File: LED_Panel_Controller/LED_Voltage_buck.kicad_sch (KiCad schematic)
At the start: 11 parts, among them U10 LM2596S-ADJ

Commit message: changed page size, BOM
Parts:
- U10: Digikey 4518-LM2596S-ADJCT-ND -> https://www.amazon.com/gp/product/B0B63GQDJW/
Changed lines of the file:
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@@
       (effects (font (size 1.27 1.27)) hide)
     )
-    (property "Digikey" "4518-LM2596S-ADJCT-ND" (id 4) (at 127 64.77 0)
+    (property "Digikey" "https://www.amazon.com/gp/product/B0B63GQDJW/" (id 4) (at 127 64.77 0)
       (effects (font (size 1.27 1.27)) hide)
     )

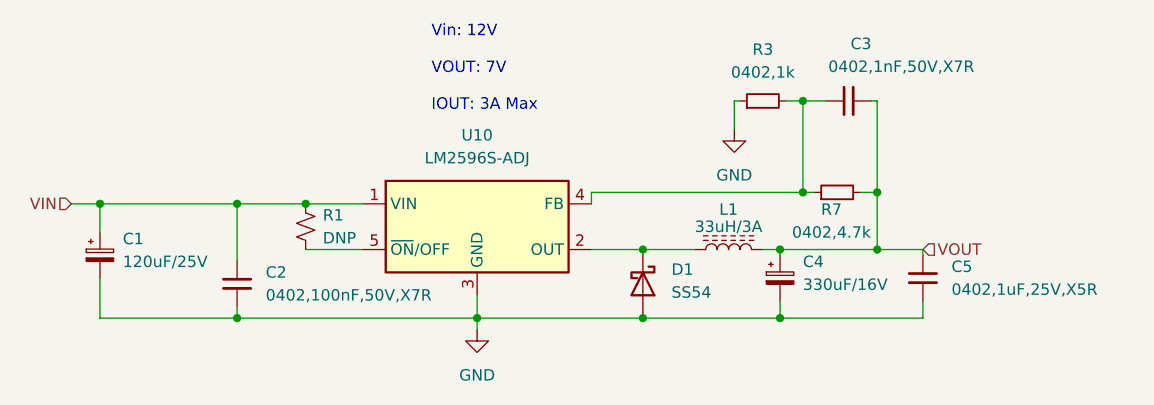
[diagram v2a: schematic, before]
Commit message: changed VIN cap to 35V rating
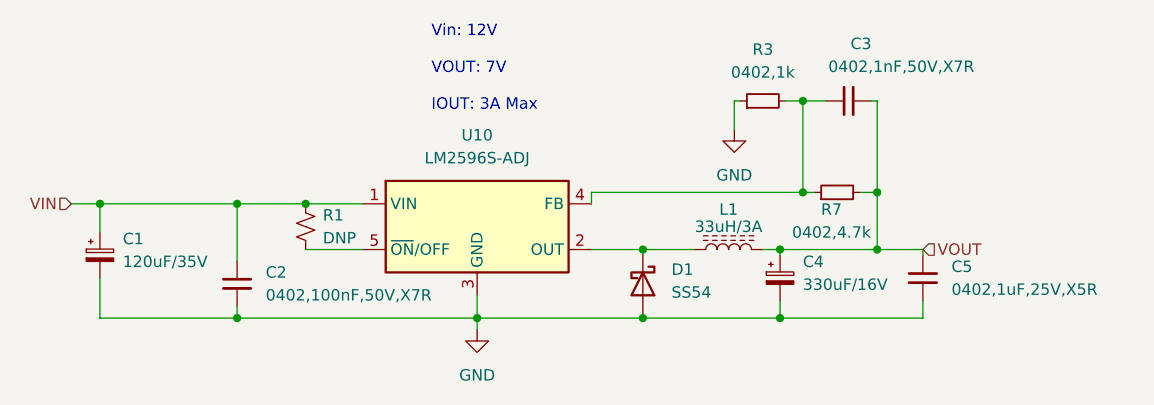
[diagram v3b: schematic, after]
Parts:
- C1: value 120uF/25V -> 120uF/35V; Digikey 732-8632-1-ND -> 1189-3657-ND; MFGPN 860010473009 -> 35ZLQ120MEFC6.3X11
- C4: Digikey 732-8798-1-ND -> 399-ESK337M016AE3AA-ND; MFGPN 860020373011 -> ESK337M016AE3AA
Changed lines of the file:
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@@
       (effects (font (size 1.27 1.27)) (justify left))
     )
-    (property "Value" "120uF/25V" (id 1) (at 87.63 68.6688 0)
+    (property "Value" "120uF/35V" (id 1) (at 87.63 68.6688 0)
       (effects (font (size 1.27 1.27)) (justify left))
     )
@@
       (effects (font (size 1.27 1.27)) hide)
     )
-    (property "Digikey" "732-8632-1-ND" (id 4) (at 85.09 67.945 0)
+    (property "Digikey" "1189-3657-ND" (id 4) (at 85.09 67.945 0)
       (effects (font (size 1.27 1.27)) hide)
     )
-    (property "MFGPN" "860010473009" (id 5) (at 85.09 67.945 0)
+    (property "MFGPN" "35ZLQ120MEFC6.3X11" (id 5) (at 85.09 67.945 0)
       (effects (font (size 1.27 1.27)) hide)
     )
@@
       (effects (font (size 1.27 1.27)) hide)
     )
-    (property "Digikey" "732-8798-1-ND" (id 4) (at 160.655 70.485 0)
+    (property "Digikey" "399-ESK337M016AE3AA-ND" (id 4) (at 160.655 70.485 0)
       (effects (font (size 1.27 1.27)) hide)
     )
-    (property "MFGPN" "860020373011" (id 5) (at 160.655 70.485 0)
+    (property "MFGPN" "ESK337M016AE3AA" (id 5) (at 160.655 70.485 0)
       (effects (font (size 1.27 1.27)) hide)
     )
